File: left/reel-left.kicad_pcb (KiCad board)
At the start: 2 copper layers, 143.2 x 92.7 mm, 49 parts, among them J1 Conn_01x02, SW1 SW_Push, SW10 SW_Push, SW11 SW_Push, SW12 SW_Push, SW13 SW_Push, SW14 SW_Push, SW15 SW_Push, SW16 SW_Push, SW17 SW_Push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

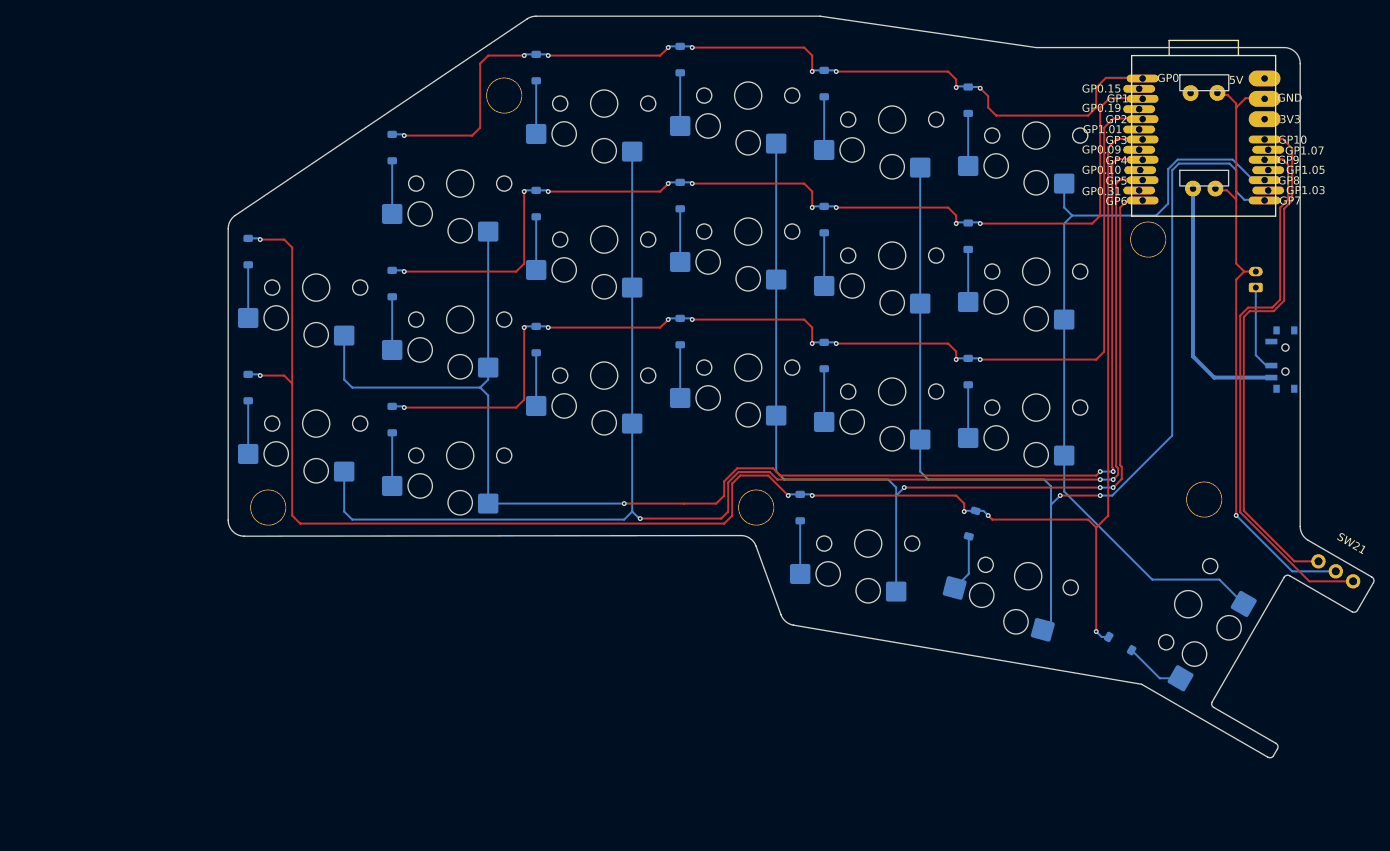
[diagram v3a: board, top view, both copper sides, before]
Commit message: Update right PCB layout
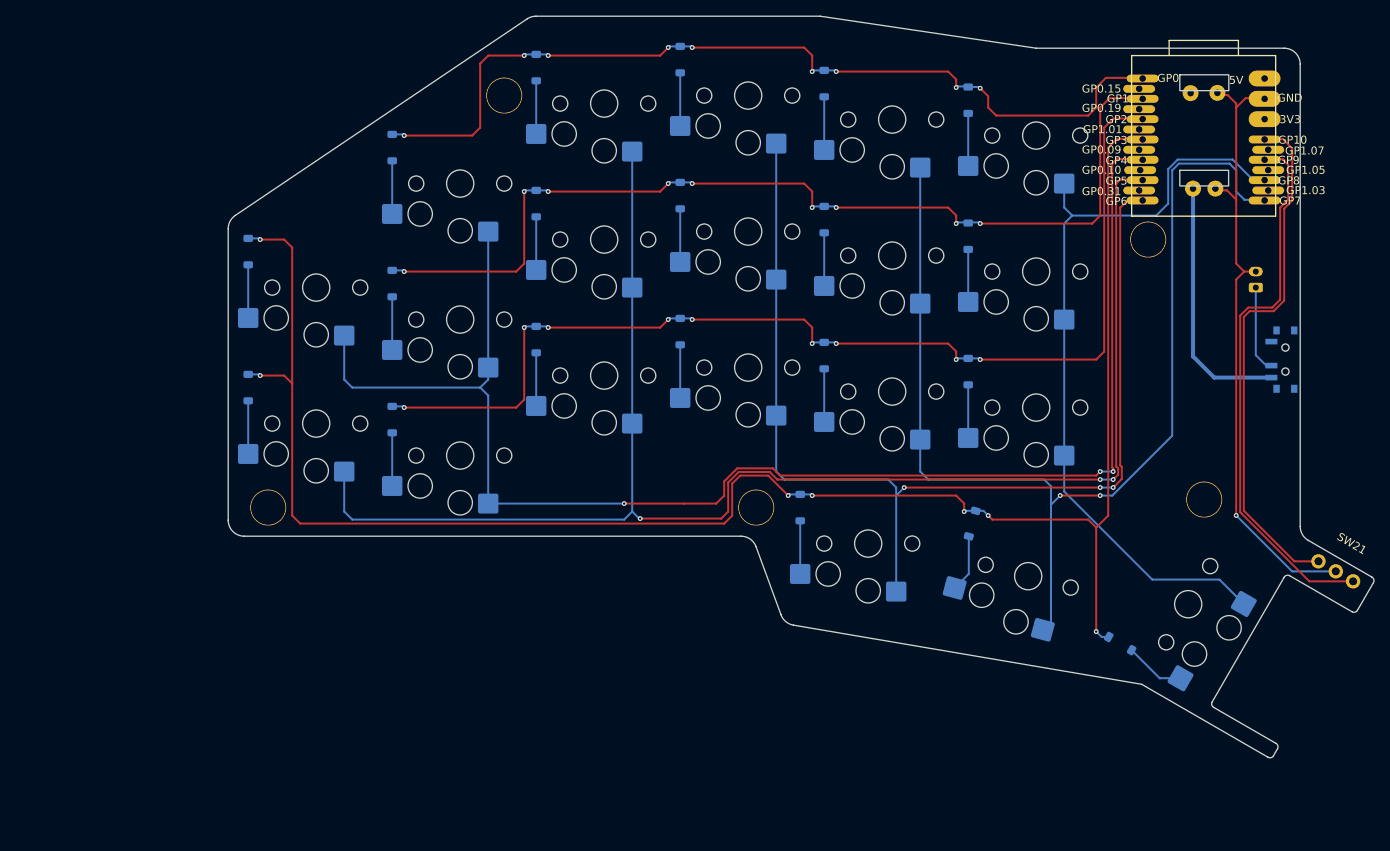
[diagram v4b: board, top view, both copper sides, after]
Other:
- outline, holes or cut-outs redrawn
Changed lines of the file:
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@@
 	(gr_line
 		(start 76.5 79.564413)
-		(end 76.5 115.997537)
+		(end 76.5 116)
 		(stroke
 			(width 0.05)
@@
 	)
 	(gr_arc
-		(start 78.502462 117.997535)
-		(mid 77.086644 117.412623)
-		(end 76.5 115.997537)
+		(start 78.5 118)
+		(mid 77.085786 117.414214)
+		(end 76.5 116)
 		(stroke
 			(width 0.05)
@@
 	)
 	(gr_line
-		(start 140.599145 117.921095)
-		(end 78.502462 117.997535)
-		(stroke
-			(width 0.05)
-			(type default)
-		)
-		(layer "Edge.Cuts")
-	)
-	(gr_arc
-		(start 140.599145 117.921095)
-		(mid 141.746519 118.282977)
-		(end 142.478732 119.237609)
-		(stroke
-			(width 0.05)
-			(type default)
-		)
-		(layer "Edge.Cuts")
-	)
-	(gr_line
-		(start 142.478732 119.237609)
+		(start 140.602982 118)
+		(end 78.5 118)
+		(stroke
+			(width 0.05)
+			(type default)
+		)
+		(layer "Edge.Cuts")
+	)
+	(gr_arc
+		(start 140.602982 118)
+		(mid 141.748265 118.360388)
+		(end 142.480802 119.311674)
+		(stroke
+			(width 0.05)
+			(type default)
+		)
+		(layer "Edge.Cuts")
+	)
+	(gr_line
+		(start 142.480802 119.311674)
 		(end 145.602368 127.827606)
 		(stroke
@@
 	)
 	(gr_line
-		(start 177.5 56.921095)
+		(start 177.5 57)
 		(end 150.5 53)
 		(stroke
@@
 	)
 	(gr_line
-		(start 208.5 56.921095)
-		(end 177.5 56.921095)
-		(stroke
-			(width 0.05)
-			(type solid)
-		)
-		(layer "Edge.Cuts")
-	)
-	(gr_arc
-		(start 208.5 56.921095)
-		(mid 209.914214 57.506881)
-		(end 210.5 58.921095)
+		(start 208.5 57)
+		(end 177.5 57)
+		(stroke
+			(width 0.05)
+			(type solid)
+		)
+		(layer "Edge.Cuts")
+	)
+	(gr_arc
+		(start 208.5 57)
+		(mid 209.914214 57.585786)
+		(end 210.5 59)
 		(stroke
 			(width 0.05)
@@
 	)
 	(gr_line
-		(start 210.5 58.921095)
+		(start 210.5 59)
 		(end 210.5 116.782527)
 		(stroke
 			(width 0.05)
-			(type default)
-		)
-		(layer "Edge.Cuts")
+			(type solid)
+		)
+		(layer "Edge.Cuts")
